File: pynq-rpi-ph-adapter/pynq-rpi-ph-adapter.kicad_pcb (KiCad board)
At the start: 2 copper layers, 167.8 x 102.7 mm, 9 parts, among them J1 Conn_02x08_Odd_Even, J2 Conn_02x08_Odd_Even, J3 Conn_02x08_Odd_Even, J4 Conn_02x08_Odd_Even, J5 Conn_02x08_Odd_Even, J6 Conn_02x08_Odd_Even, J7 Conn_02x20_Odd_Even

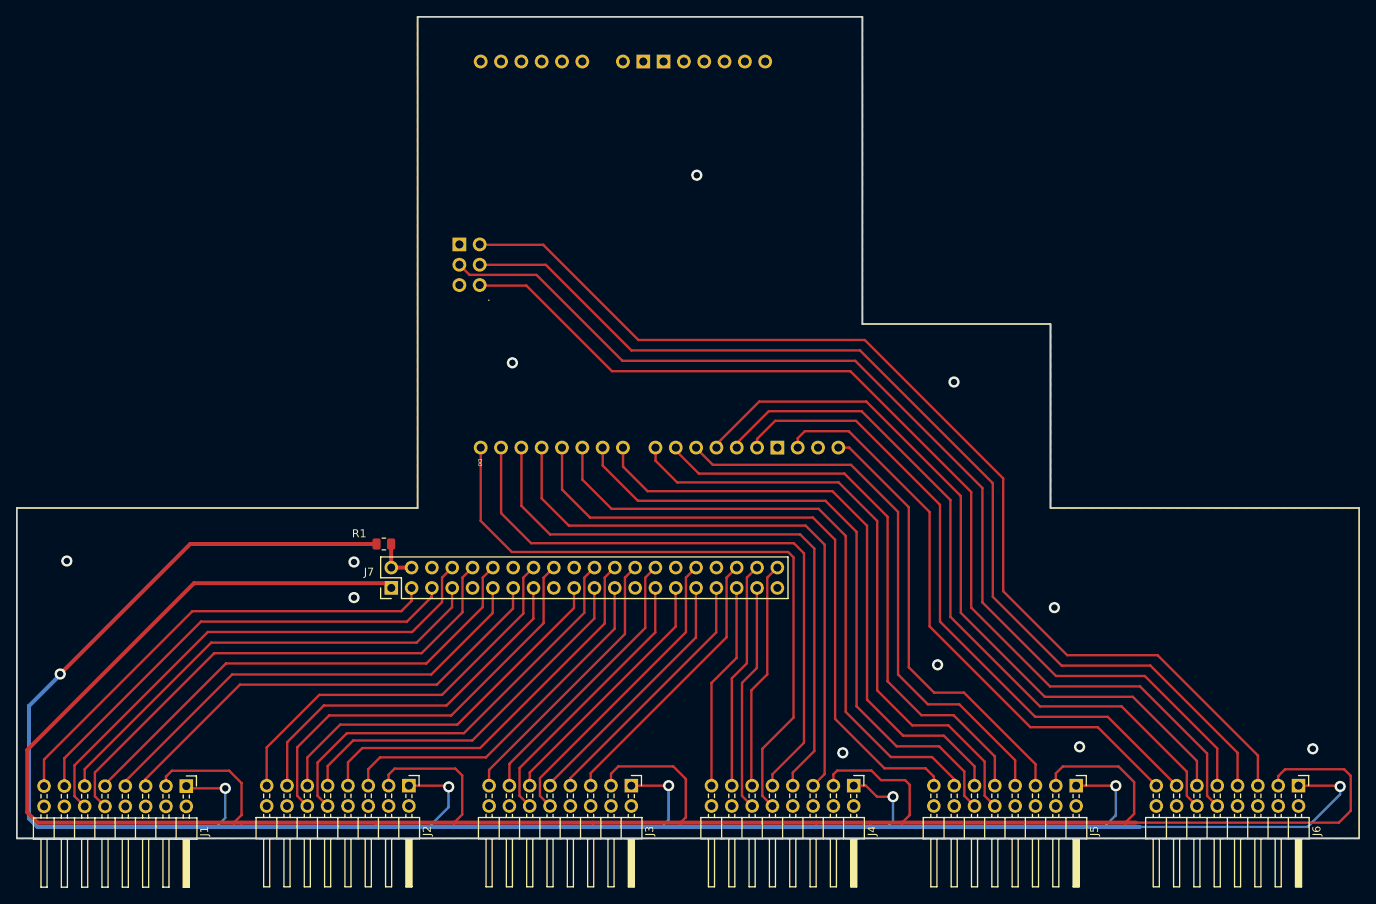
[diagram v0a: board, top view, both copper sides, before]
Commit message: Adapted and generated gerber files for pynq rpi adapter for jlcpcb
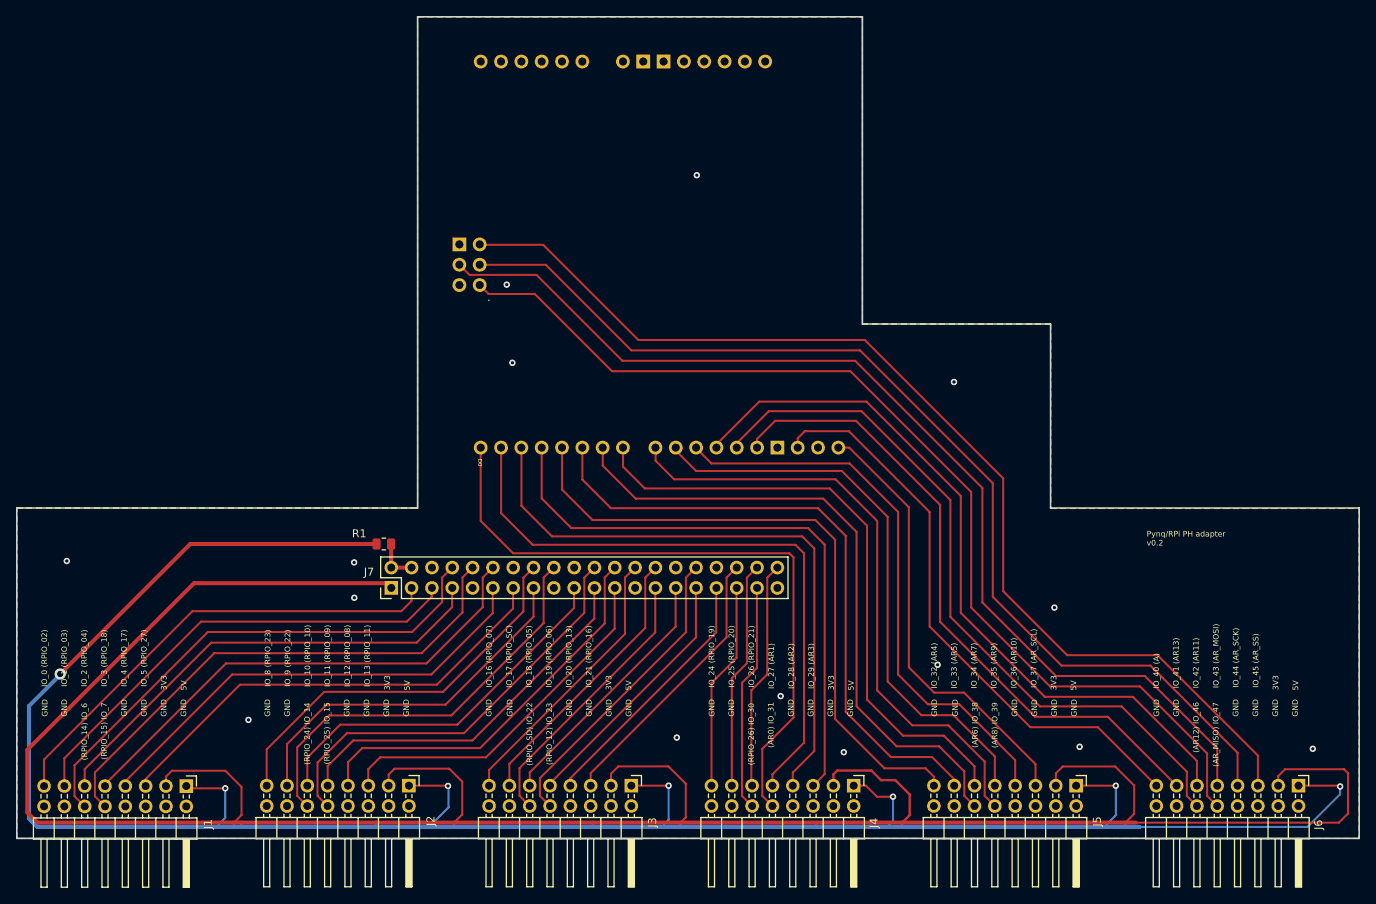
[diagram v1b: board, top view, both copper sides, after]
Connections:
- J2 pad 13: /IO_8 -> /IO_9
- J2 pad 15: /IO_9 -> /IO_8
- J7 pad 15: /IO_8 -> /IO_9
- J7 pad 16: /IO_9 -> /IO_8
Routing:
- net /IO_9: track 50.1 -> 46.2 mm
- net /IO_8: track 46.5 -> 49.8 mm
- net +3V3: track 331.2 -> 328.8 mm
- net GND: vias 11 -> 15
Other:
- board text added: "(AR0) IO_31"
- board text added: "(AR12) IO_46"
- board text added: "(AR6) IO_38"
- board text added: "(AR8) IO_39"
- board text added: "(AR_MISO) IO_47"
- board text added: "(RPIO_12) IO_23"
- board text added: "(RPIO_14) IO_6"
- board text added: "(RPIO_15) IO_7"
- board text added: "(RPIO_24) IO_14"
- board text added: "(RPIO_25) IO_15"
- board text added: "(RPIO_26) IO_30"
- board text added: "(RPIO_SD) IO_22"
- board text added: "3V3"
- board text added: "5V"
- board text added: "GND"
- board text added: "IO_0 (RPIO_02)"
- board text added: "IO_1 (RPIO_03)"
- board text added: "IO_10 (RPIO_10)"
- board text added: "IO_11 (RPIO_09)"
- board text added: "IO_12 (RPIO_08)"
- board text added: "IO_13 (RPIO_11)"
- board text added: "IO_16 (RPIO_07)"
- board text added: "IO_17 (RPIO_SC)"
- board text added: "IO_18 (RPIO_05)"
- board text added: "IO_19 (RPIO_06)"
- board text added: "IO_2 (RPIO_04)"
- board text added: "IO_20 (RPIO_13)"
- board text added: "IO_21 (RPIO_16)"
- board text added: "IO_24 (RPIO_19)"
- board text added: "IO_25 (RPIO_20)"
- board text added: "IO_26 (RPIO_21)"
- board text added: "IO_27 (AR1)"
- board text added: "IO_28 (AR2)"
- board text added: "IO_29 (AR3)"
- board text added: "IO_3 (RPIO_18)"
- board text added: "IO_32 (AR4)"
- board text added: "IO_33 (AR5)"
- board text added: "IO_34 (AR7)"
- board text added: "IO_35 (AR9)"
- board text added: "IO_36 (AR10)"
- board text added: "IO_37 (AR_SCL)"
- board text added: "IO_4 (RPIO_17)"
- board text added: "IO_40 (A)"
- board text added: "IO_41 (AR13)"
- board text added: "IO_42 (AR11)"
- board text added: "IO_43 (AR_MOSI)"
- board text added: "IO_44 (AR_SCK)"
- board text added: "IO_45 (AR_SS)"
- board text added: "IO_5 (RPIO_27)"
- board text added: "IO_8 (RPIO_23)"
- board text added: "IO_9 (RPIO_22)"
- board text added: "Pynq/RPi PH adapter v0.2"
